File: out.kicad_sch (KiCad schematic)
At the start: 77 parts, among them J1 IN_L, J2 POWER, J3 IN_R, J4 IN_CUE, J5 STEREO_OUT, J6 PHONE_OUT, Q1 MMBT3904, Q2 MMBT3904, Q3 MMBT3904, SW1 PHONE_SELECTOR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

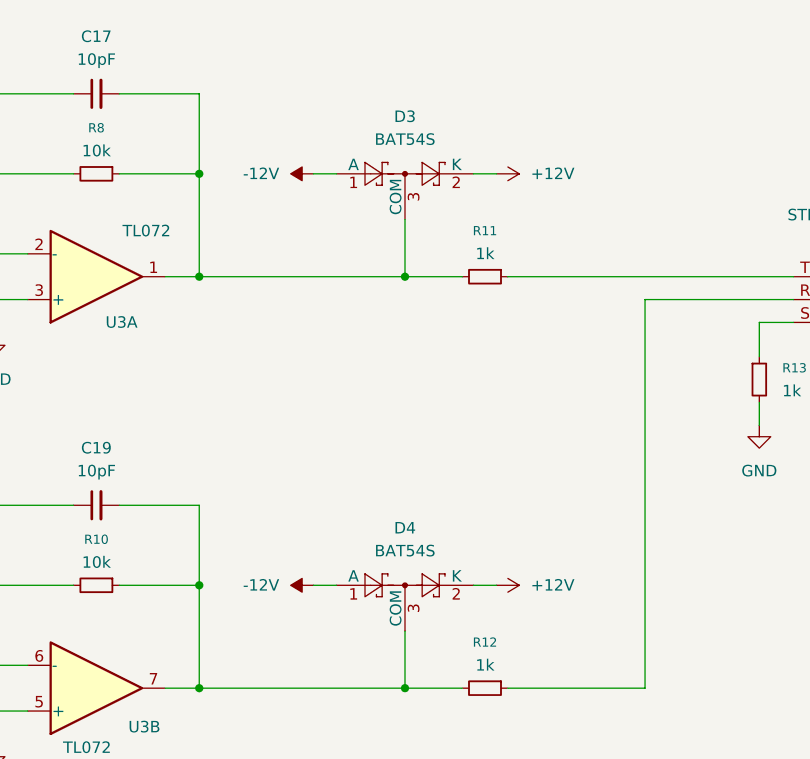
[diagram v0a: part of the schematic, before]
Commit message: feat: route power planes
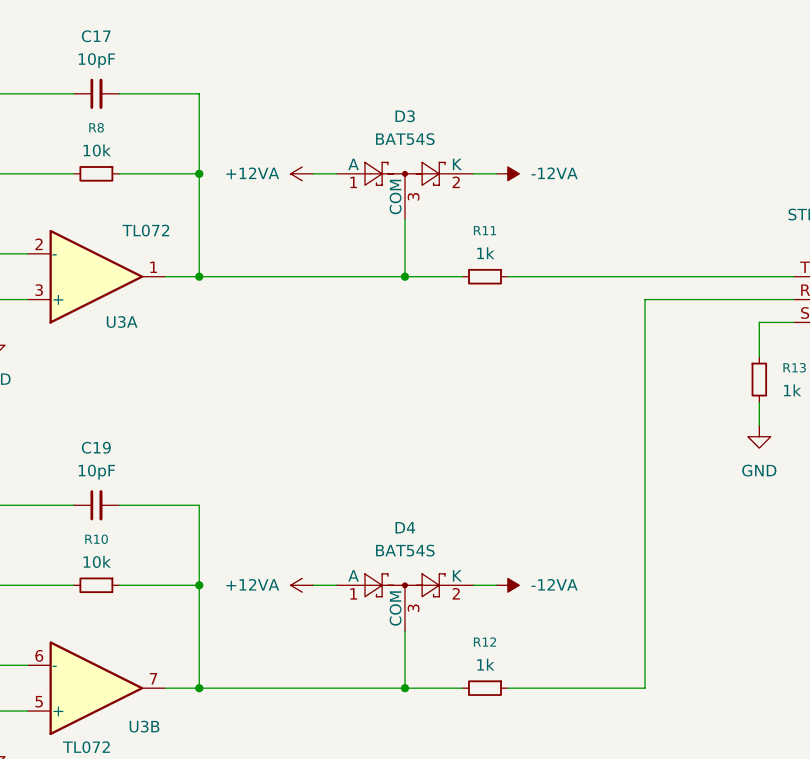
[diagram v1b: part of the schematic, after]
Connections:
- net +12V: no longer D3.2 (K), D4.2 (K)
- net +12VA: now also D3.1 (A), D4.1 (A)
- net -12V: no longer D3.1 (A), D4.1 (A)
- net -12VA: now also D3.2 (K), D4.2 (K)

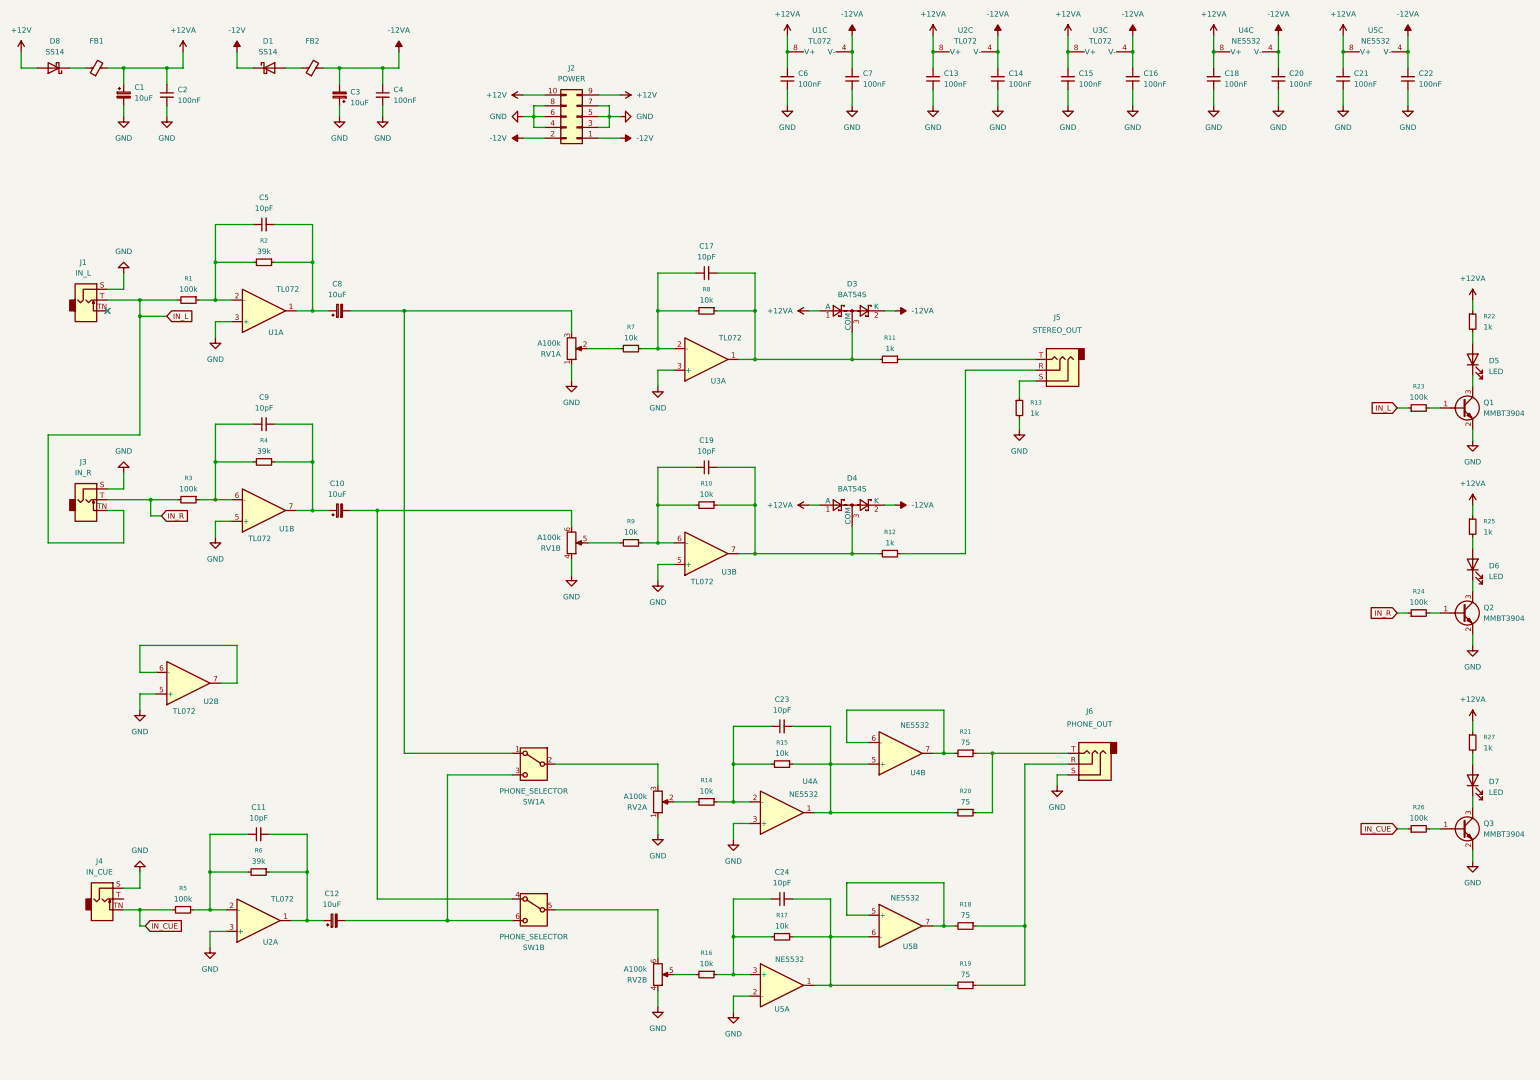
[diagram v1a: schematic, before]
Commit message: doc: add errors found in first build
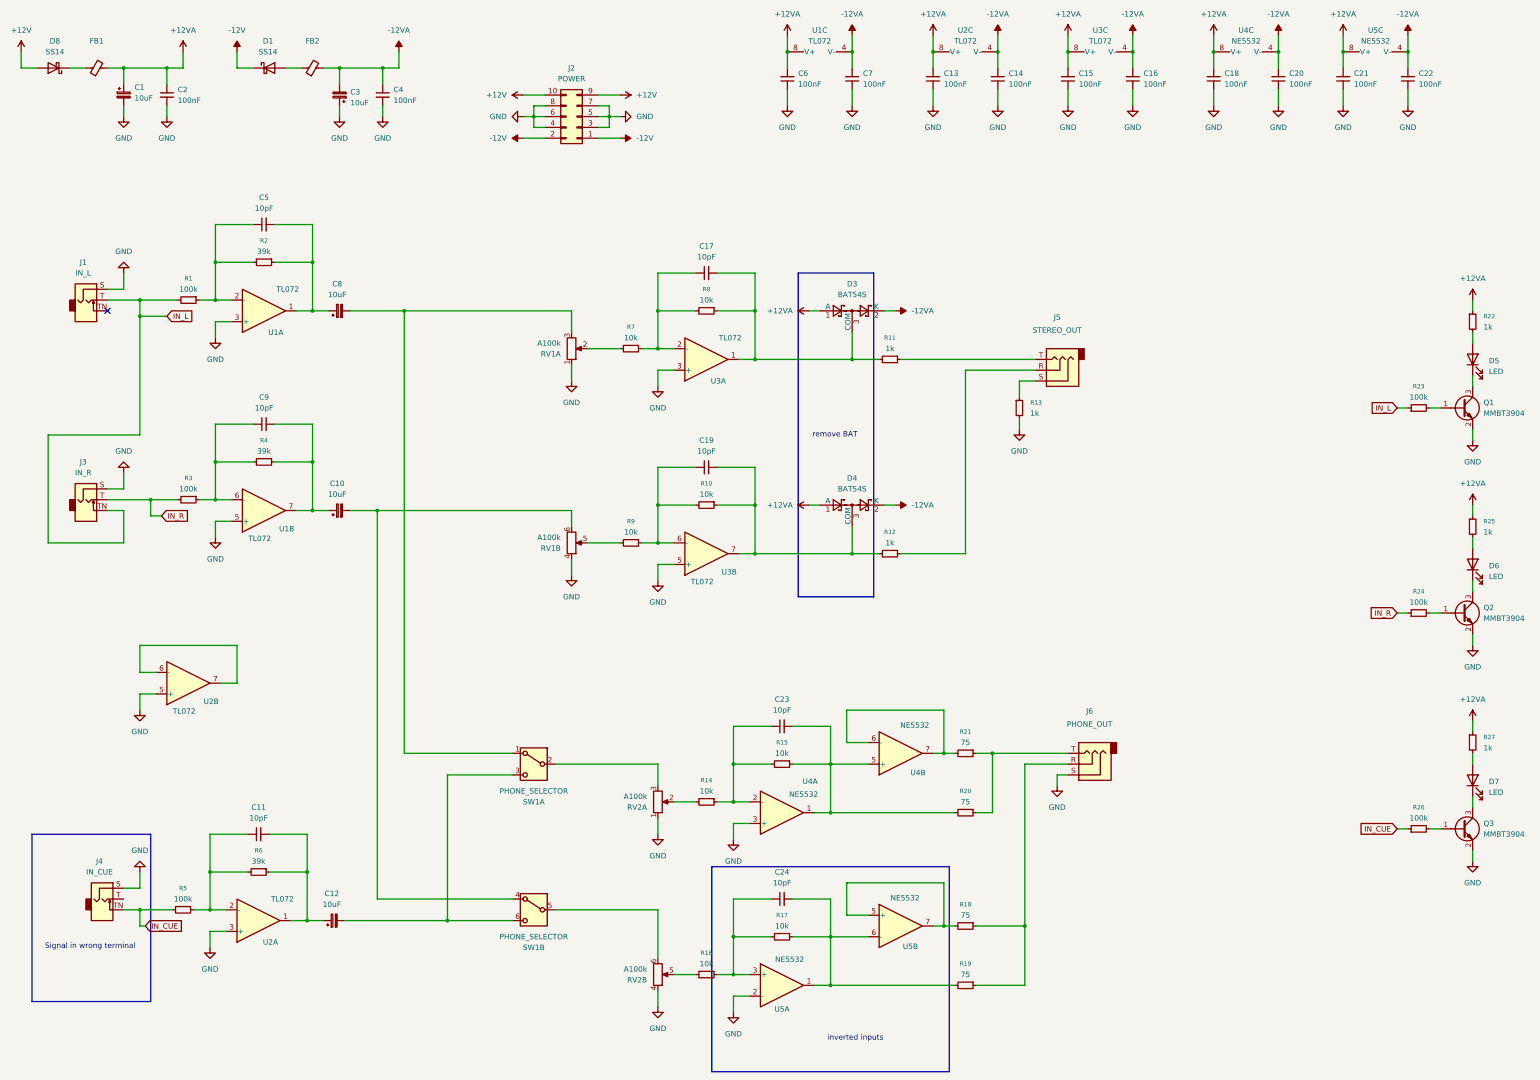
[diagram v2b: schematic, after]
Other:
- note added: "Signal in wrong terminal"
- note added: "inverted inputs"
- note added: "remove BAT"
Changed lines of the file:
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@@
 	(generator_version "9.0")
 	(paper "A3")
+	(rectangle
+		(start 27.94 218.44)
+		(end 55.88 257.81)
+		(stroke
+			(width 0)
+			(type default)
+		)
+		(fill
+			(type none)
+		)
+	)
+	(rectangle
+		(start 187.96 226.06)
+		(end 243.84 274.32)
+		(stroke
+			(width 0)
+			(type default)
+		)
+		(fill
+			(type none)
+		)
+	)
+	(rectangle
+		(start 208.28 86.36)
+		(end 226.06 162.56)
+		(stroke
+			(width 0)
+			(type default)
+		)
+		(fill
+			(type none)
+		)
+	)
+	(text "remove BAT"
+		(exclude_from_sim no)
+		(at 216.916 124.46 0)
+		(effects
+			(font
+				(size 1.27 1.27)
+			)
+		)
+	)
+	(text "Signal in wrong terminal"
+		(exclude_from_sim no)
+		(at 41.656 244.856 0)
+		(effects
+			(font
+				(size 1.27 1.27)
+			)
+		)
+	)
+	(text "inverted inputs"
+		(exclude_from_sim no)
+		(at 221.742 266.446 0)
+		(effects
+			(font
+				(size 1.27 1.27)
+			)
+		)
+	)
 	(junction
 		(at 215.9 254)

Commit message: fix: correct errors found in release 1.0.0
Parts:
- removed D3, D4: BAT54S, Package_TO_SOT_SMD:SOT-23, symbol Diode:BAT54S
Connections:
- net GND: now also U5.3 (+); no longer U5.2 (-)
- net IN_CUE: now also J4.T; no longer J4.TN
- net at C24.2, R17.1, R19.2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: now also U5.5 (+); no longer U5.6 (-)
- net at C24.1, R16.1, R17.2: now also U5.2 (-); no longer U5.3 (+)
- net at R18.2, U5.7: now also U5.6 (-); no longer U5.5 (+)
- no-connect marks 1 -> 2
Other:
- note removed: "Signal in wrong terminal"
- note removed: "inverted inputs"
- note removed: "remove BAT"
- moved on the sheet: J4

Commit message: feat: adapt pcb to two layers, fix opamp and jack routing
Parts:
- added D2, D3: BAT54S, Package_TO_SOT_SMD:SOT-23, symbol Diode:BAT54S
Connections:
- net +12VA: now also D2.2 (K), D3.2 (K)
- net -12VA: now also D2.1 (A), D3.1 (A)
- net at C19.2, R10.1, R12.2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: now also D3.3 (COM)
- net at C17.2, R11.2, R8.1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: now also D2.3 (COM)
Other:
- title: (none) -> Raw output
- moved on the sheet: R11, R12
